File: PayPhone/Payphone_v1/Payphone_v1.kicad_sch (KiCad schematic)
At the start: 29 parts, among them J1 JST_05, J2 Molex_26-60-4030, J3 Molex_26-60-4040, J4 HV_SELECT, J5 SPARE_IO, J6 PINHD_1x5_Male, J7 PINHD_1x2_Male, K1 G6S-2, Q1 IRF630, Q2 2N7000, Q3 IRF630, Q4 2N7000, Q5 2N7000, U1 MCP23008-xP, U2 MC34063AP, U3 UC3843AN

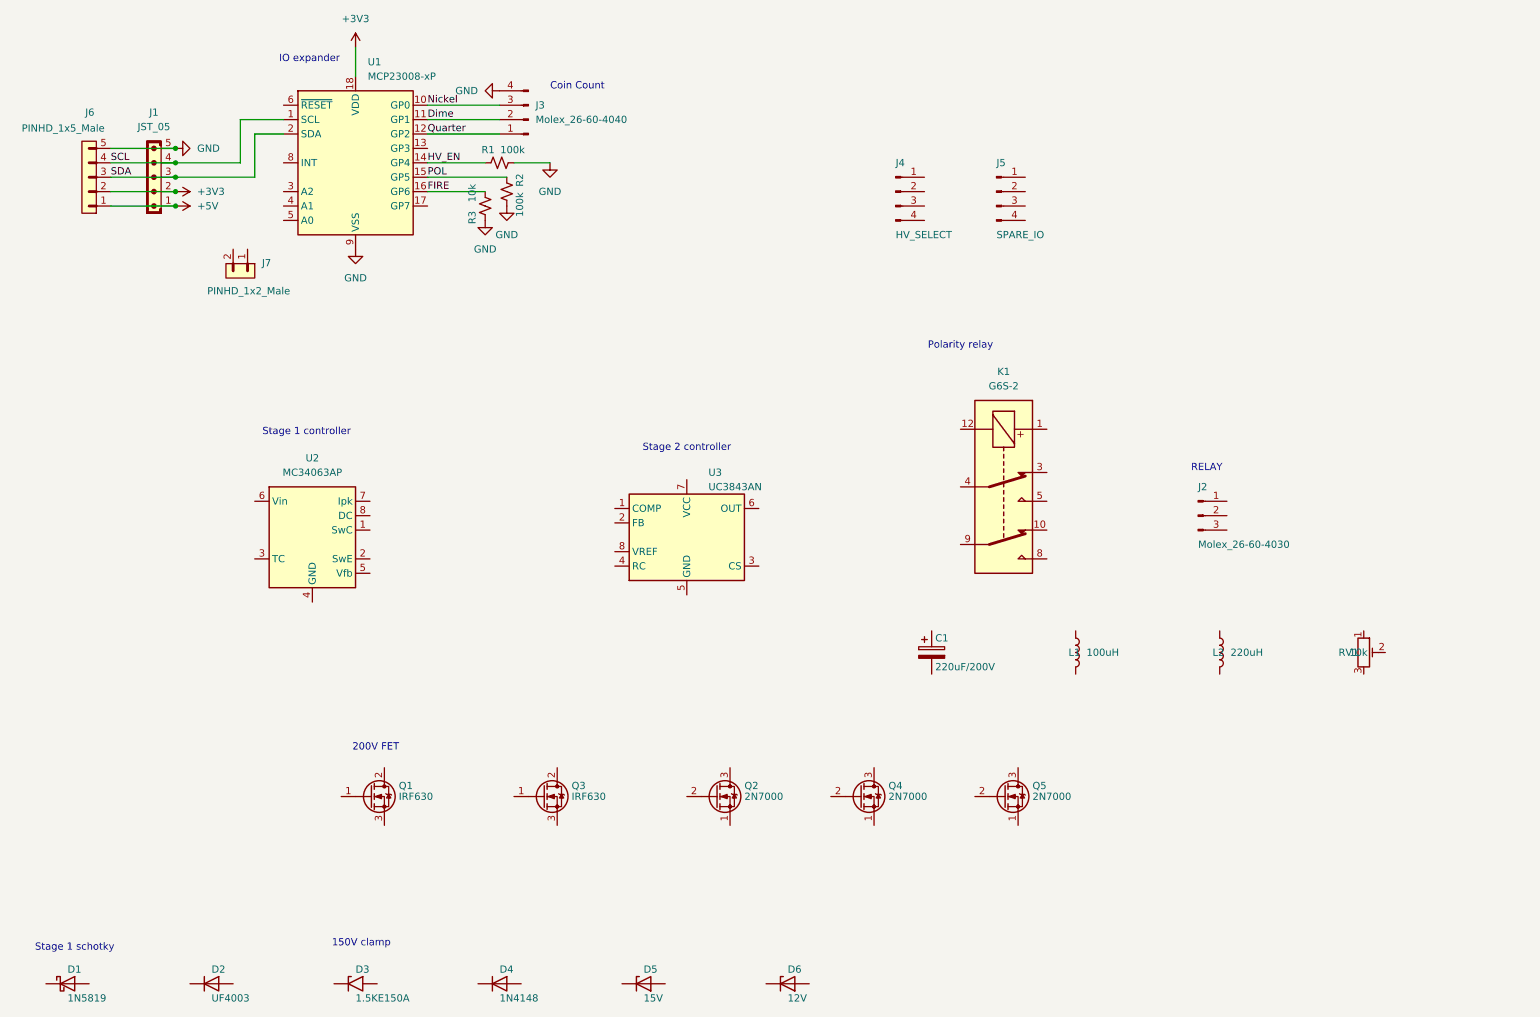
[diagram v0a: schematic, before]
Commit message: modified:   CLAUDE.md 	modified:   PayPhone/Payphone_v1/Payphone_v1.kicad_pro 	modified:   PayPhone/Payphone_v1/Payphone_v1.kicad_sch 	modified:   PayPhone/coin-board-schematic.md
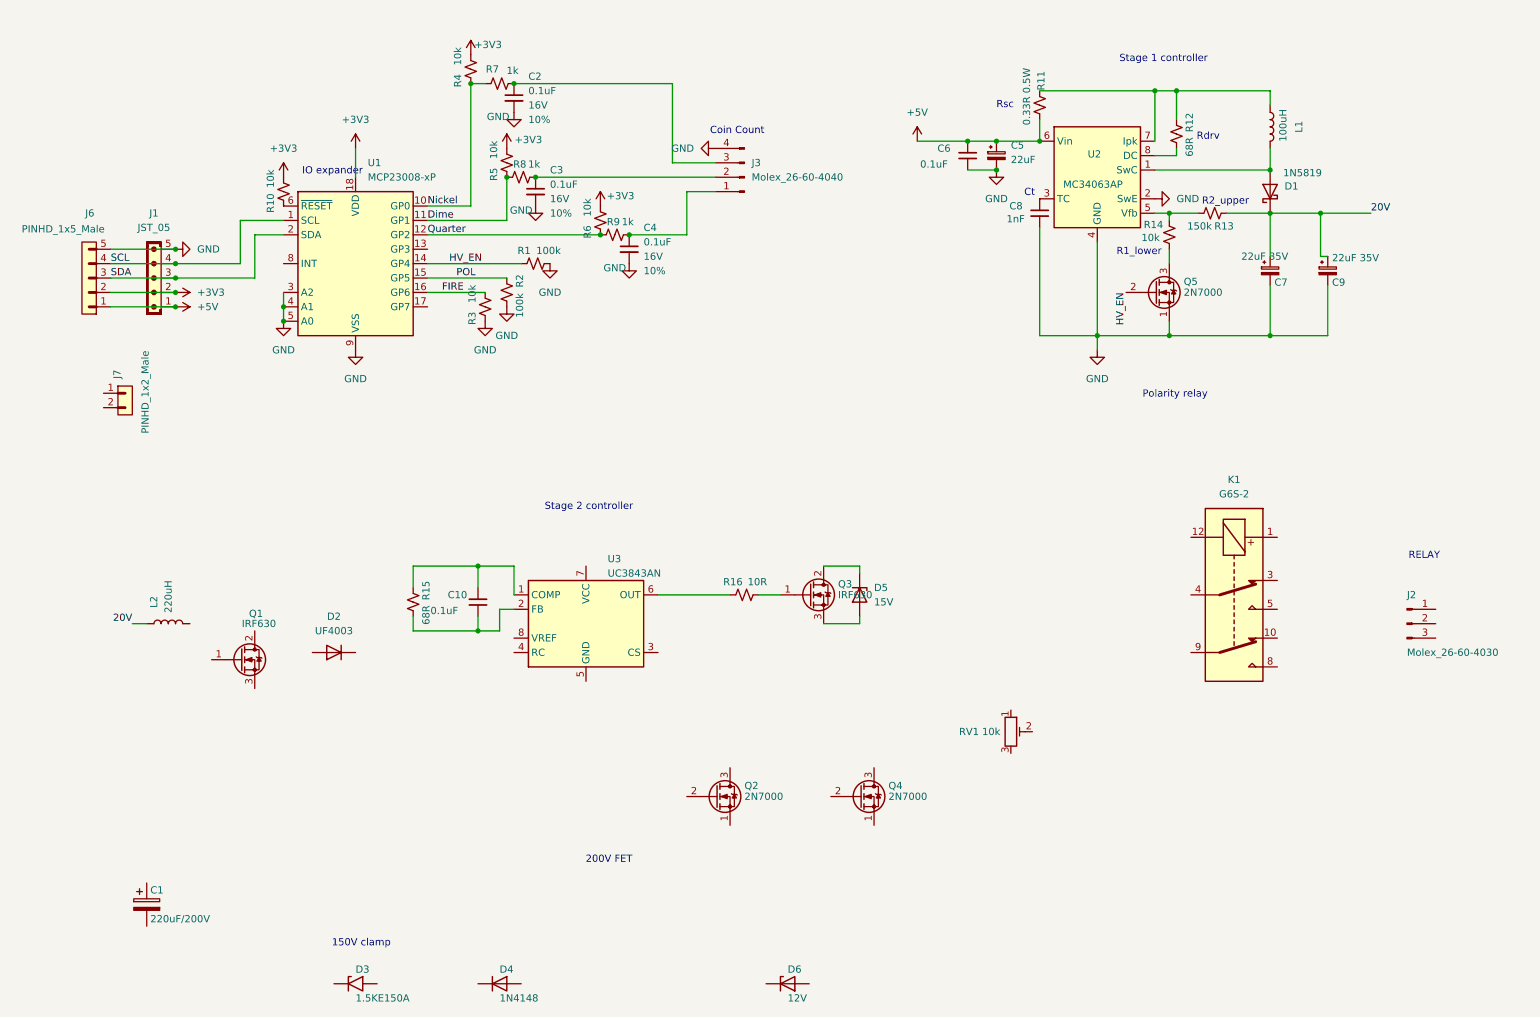
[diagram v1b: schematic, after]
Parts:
- removed J4: HV_SELECT, Connector_PinHeader_2.54mm:PinHeader_1x04_P2.54mm_Vertical, symbol Connector:Conn_01x04_Pin
- removed J5: SPARE_IO, Connector_PinHeader_2.54mm:PinHeader_1x04_P2.54mm_Vertical, symbol Connector:Conn_01x04_Pin
- added C10, C6: 0.1uF, Capacitor_THT:C_Disc_D10.0mm_W2.5mm_P5.00mm, symbol Device:C_Small
- added C2, C3, C4: 0.1uF, Capacitor_THT:C_Disc_D10.0mm_W2.5mm_P5.00mm, symbol PCM_SparkFun-Capacitor:1.0uF_0402_16V_10%
- added C5: 22uF, Capacitor_THT:CP_Radial_D5.0mm_P2.00mm, symbol Device:C_Polarized_Small
- added C7, C9: 22uF 35V, Capacitor_THT:CP_Radial_D5.0mm_P2.00mm, symbol Device:C_Polarized_Small
- added C8: 1nF, Capacitor_THT:C_Disc_D10.0mm_W2.5mm_P5.00mm, symbol Device:C_Small
- added R10, R14, R4, R5, R6: 10k, PCM_SparkFun-Resistor:R_0603_1608Metric, symbol PCM_SparkFun-Resistor:R_Small
- added R11: 0.33R 0.5W, PCM_SparkFun-Resistor:R_0603_1608Metric, symbol PCM_SparkFun-Resistor:R_Small
- added R12, R15: 68R, PCM_SparkFun-Resistor:R_0603_1608Metric, symbol PCM_SparkFun-Resistor:R_Small
- added R13: 150k, PCM_SparkFun-Resistor:R_0603_1608Metric, symbol PCM_SparkFun-Resistor:R_Small
- added R16: 10R, PCM_SparkFun-Resistor:R_0603_1608Metric, symbol PCM_SparkFun-Resistor:R_Small
- added R7, R8, R9: 1k, PCM_SparkFun-Resistor:R_0402_1005Metric, symbol PCM_SparkFun-Resistor:R_Small
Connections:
- net +3V3: now also R10.1, R4.1, R5.1, R6.1
- net +5V: now also U2.6 (Vin), C5.1, C6.2, R11.2
- net Dime: now also R5.2, R8.2; no longer J3.2 (Pin_2)
- net GND: now also Q5.1 (S), U1.3 (A2), U1.4 (A1), U1.5 (A0), U2.2 (SwE), U2.4 (GND), C2.2, C3.2, C4.2, C5.2, C6.1, C7.2, C8.1, C9.2
- net HV_EN: now also Q5.2 (G)
- net Nickel: now also R4.2, R7.2; no longer J3.3 (Pin_3)
- net Quarter: now also R6.2, R9.2; no longer J3.1 (Pin_1)
- net at U3.1 (COMP): now also C10.2, R15.2
- net at U3.2 (FB): now also C10.1, R15.1
- net at U3.6 (OUT): now also R16.2
- net 20V: now reaches D1.1 (K)
- net 20V: now also L2.1, C7.1, C9.1, R13.2
- net at D1.2 (A): now also L1.2, U2.1 (SwC)
- net at U2.3 (TC): now also C8.2
- net at U2.5 (Vfb): now also R13.1, R14.1
- net at U2.7 (Ipk): now also L1.1, R11.1, R12.2
- net at U2.8 (DC): now also R12.1
- net at U1.6 (~{RESET}): now also R10.2
- net at D5.1 (K): now also Q3.2 (D)
- net at D5.2 (A): now also Q3.3 (S)
- net at Q5.3 (D): now also R14.2
- net at Q3.1 (G): now also R16.1
- new net: C3.1, J3.2 (Pin_2), R8.1
- new net: C4.1, J3.1 (Pin_1), R9.1
- new net: C2.1, J3.3 (Pin_3), R7.1
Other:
- note added: "Ct"
- note added: "R1_lower"
- note added: "R2_upper"
- note added: "Rdrv"
- note added: "Rsc"
- note removed: "Stage 1 schotky"
- moved on the sheet: C1, D1, D2, D5, J1, J2, J3, J6, J7, K1, L1, L2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

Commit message: modified:   PayPhone/Payphone_v1/Payphone_v1.kicad_pro 	modified:   PayPhone/Payphone_v1/Payphone_v1.kicad_sch
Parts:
- added C11: 2.2nF, Capacitor_THT:C_Disc_D10.0mm_W2.5mm_P5.00mm, symbol Device:C_Small
- added C12, C13: 0.1uF, Capacitor_THT:C_Disc_D10.0mm_W2.5mm_P5.00mm, symbol Device:C_Small
- added R17: 2R 1W, PCM_SparkFun-Resistor:R_0603_1608Metric, symbol PCM_SparkFun-Resistor:R_Small
- added R18: 12k, PCM_SparkFun-Resistor:R_0603_1608Metric, symbol PCM_SparkFun-Resistor:R_Small
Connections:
- net 20V: now also U3.7 (VCC), C12.2
- net GND: now also C11.1, C12.1, C13.1
- net at U3.4 (RC): now also C11.2, R18.2
- net at U3.8 (VREF): now also C13.2, R18.1
- net at D5.2 (A), Q3.3 (S): now also R17.2
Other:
- note added: "Ca"
- note added: "Ra"
- note added: "Rcs"
- note added: "Rg"
- note added: "Rt"
- moved on the sheet: D2

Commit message: Update for new schematic
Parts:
- renumbered Q1 to Qa
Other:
- moved on the sheet: C1, D3, D4, D6
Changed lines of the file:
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@@
 	(text "200V FET"
 		(exclude_from_sim no)
-		(at 123.444 163.576 0)
+		(at 145.288 143.764 0)
 		(effects
 			(font
@@
 	(text "150V clamp\n"
 		(exclude_from_sim no)
-		(at 79.756 178.308 0)
+		(at 87.376 159.258 0)
 		(effects
 			(font
@@
 	(symbol
 		(lib_id "Diode:1N4148")
-		(at 104.14 185.42 0)
+		(at 106.68 167.64 0)
 		(unit 1)
 		(body_style 1)
@@
 		(fields_autoplaced yes)
 		(property "Reference" "D4"
-			(at 104.14 182.88 0)
+			(at 106.68 165.1 0)
 			(show_name no)
 			(do_not_autoplace no)
@@
 		)
 		(property "Value" "1N4148"
-			(at 104.14 187.96 0)
+			(at 106.68 170.18 0)
 			(show_name no)
 			(do_not_autoplace no)
@@
 		)
 		(property "Footprint" "Diode_THT:D_DO-35_SOD27_P7.62mm_Horizontal"
-			(at 104.14 195.42 0)
+			(at 106.68 177.64 0)
 			(hide yes)
 			(show_name no)
@@
 		)
 		(property "Datasheet" "https://assets.nexperia.com/documents/data-sheet/1N4148_1N4448.pdf"
-			(at 104.14 195.42 0)
+			(at 106.68 177.64 0)
 			(hide yes)
 			(show_name no)
@@
 		)
 		(property "Description" "100V 0.15A standard switching diode, DO-35"
-			(at 104.14 185.42 0)
+			(at 106.68 167.64 0)
 			(hide yes)
 			(show_name no)
@@
 	(symbol
 		(lib_id "Device:D_Zener")
-		(at 154.94 185.42 0)
+		(at 124.46 167.64 0)
 		(unit 1)
 		(body_style 1)
@@
 		(fields_autoplaced yes)
 		(property "Reference" "D6"
-			(at 154.94 182.88 0)
+			(at 124.46 165.1 0)
 			(show_name no)
 			(do_not_autoplace no)
@@
 		)
 		(property "Value" "12V"
-			(at 154.94 187.96 0)
+			(at 124.46 170.18 0)
 			(show_name no)
 			(do_not_autoplace no)
@@
 		)
 		(property "Footprint" "Diode_THT:D_DO-41_SOD81_P10.16mm_Horizontal"
-			(at 154.94 195.42 0)
+			(at 124.46 177.64 0)
 			(hide yes)
 			(show_name no)
@@
 		)
 		(property "Datasheet" ""
-			(at 154.94 195.42 0)
+			(at 124.46 177.64 0)
 			(hide yes)
 			(show_name no)
@@
 		)
 		(property "Description" "Zener diode"
-			(at 154.94 185.42 0)
+			(at 124.46 167.64 0)
 			(hide yes)
 			(show_name no)
@@
 	(symbol
 		(lib_id "Device:C_Polarized")
-		(at 41.91 171.45 0)
+		(at 66.04 163.83 0)
 		(unit 1)
 		(body_style 1)
@@
 		(fields_autoplaced yes)
 		(property "Reference" "C1"
-			(at 42.545 168.91 0)
+			(at 66.675 161.29 0)
 			(show_name no)
 			(do_not_autoplace no)
@@
 		)
 		(property "Value" "220uF/200V"
-			(at 42.545 173.99 0)
+			(at 66.675 166.37 0)
 			(show_name no)
 			(do_not_autoplace no)
@@
 		)
 		(property "Footprint" "Capacitor_THT:CP_Radial_D18.0mm_P7.50mm"
-			(at 41.91 181.45 0)
+			(at 66.04 173.83 0)
 			(hide yes)
 			(show_name no)
@@
 		)
 		(property "Datasheet" ""
-			(at 41.91 181.45 0)
+			(at 66.04 173.83 0)
 			(hide yes)
 			(show_name no)
@@
 		)
 		(property "Description" "Polarized capacitor"
-			(at 41.91 171.45 0)
+			(at 66.04 163.83 0)
 			(hide yes)
 			(show_name no)
@@
 		(in_pos_files yes)
 		(dnp no)
-		(property "Reference" "Q1"
+		(property "Reference" "Qa"
 			(at 59.944 120.142 0)
 			(show_name no)
@@
 			(project "Payphone_v1"
 				(path "/65d67a88-28a0-4b0c-a749-df348fda1ee9"
-					(reference "Q1")
+					(reference "Qa")
 					(unit 1)
 				)
@@
 	(symbol
 		(lib_id "Diode:1.5KExxA")
-		(at 78.74 185.42 0)
+		(at 86.36 166.37 0)
 		(unit 1)
 		(body_style 1)
@@
 		(fields_autoplaced yes)
 		(property "Reference" "D3"
-			(at 78.74 182.88 0)
+			(at 86.36 163.83 0)
 			(show_name no)
 			(do_not_autoplace no)
@@
 		)
 		(property "Value" "1.5KE150A"
-			(at 78.74 187.96 0)
+			(at 86.36 168.91 0)
 			(show_name no)
 			(do_not_autoplace no)
@@
 		)
 		(property "Footprint" "Diode_THT:D_DO-201AD_P15.24mm_Horizontal"
-			(at 78.74 195.42 0)
+			(at 86.36 176.37 0)
 			(hide yes)
 			(show_name no)
@@
 		)
 		(property "Datasheet" "https://www.vishay.com/docs/88301/15ke.pdf"
-			(at 78.74 195.42 0)
+			(at 86.36 176.37 0)
 			(hide yes)
 			(show_name no)
@@
 		)
 		(property "Description" "1500W unidirectional TVS diode, DO-201AE"
-			(at 78.74 185.42 0)
+			(at 86.36 166.37 0)
 			(hide yes)
 			(show_name no)
